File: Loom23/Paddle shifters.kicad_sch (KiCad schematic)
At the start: 0 parts

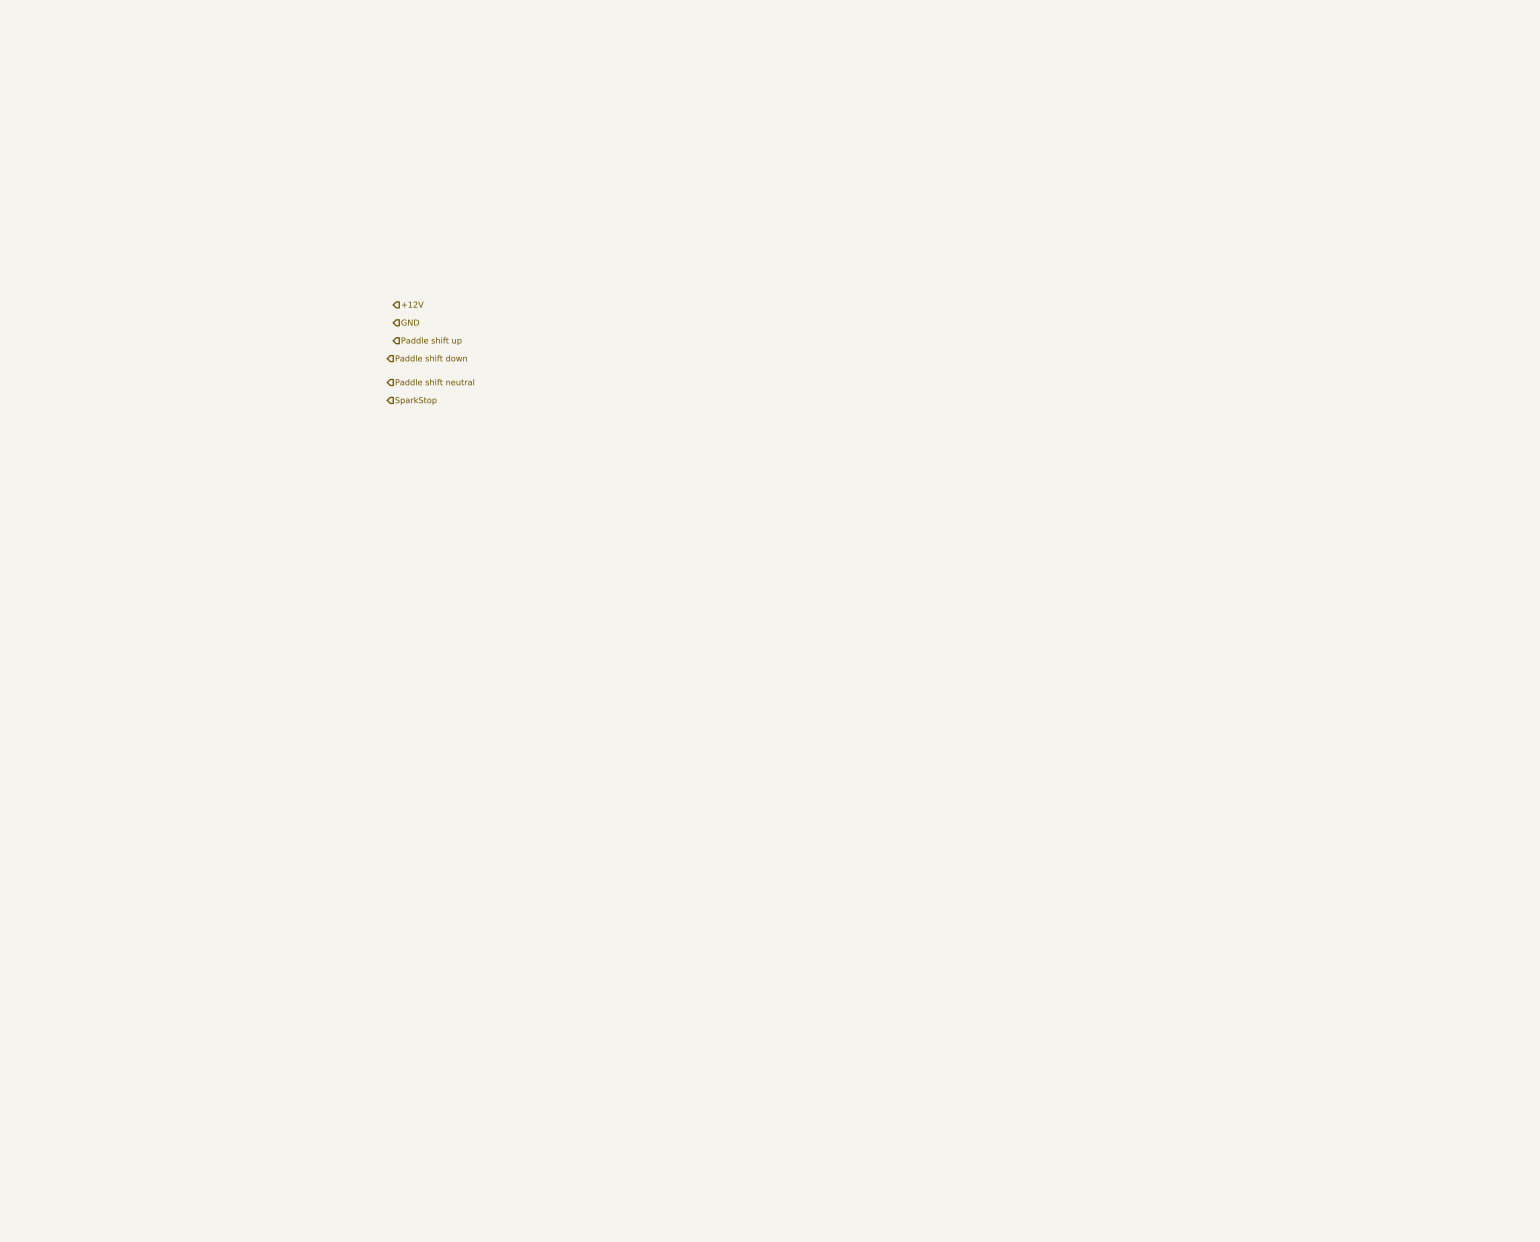
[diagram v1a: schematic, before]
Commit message: Added paddle shifter PCB and the relays.
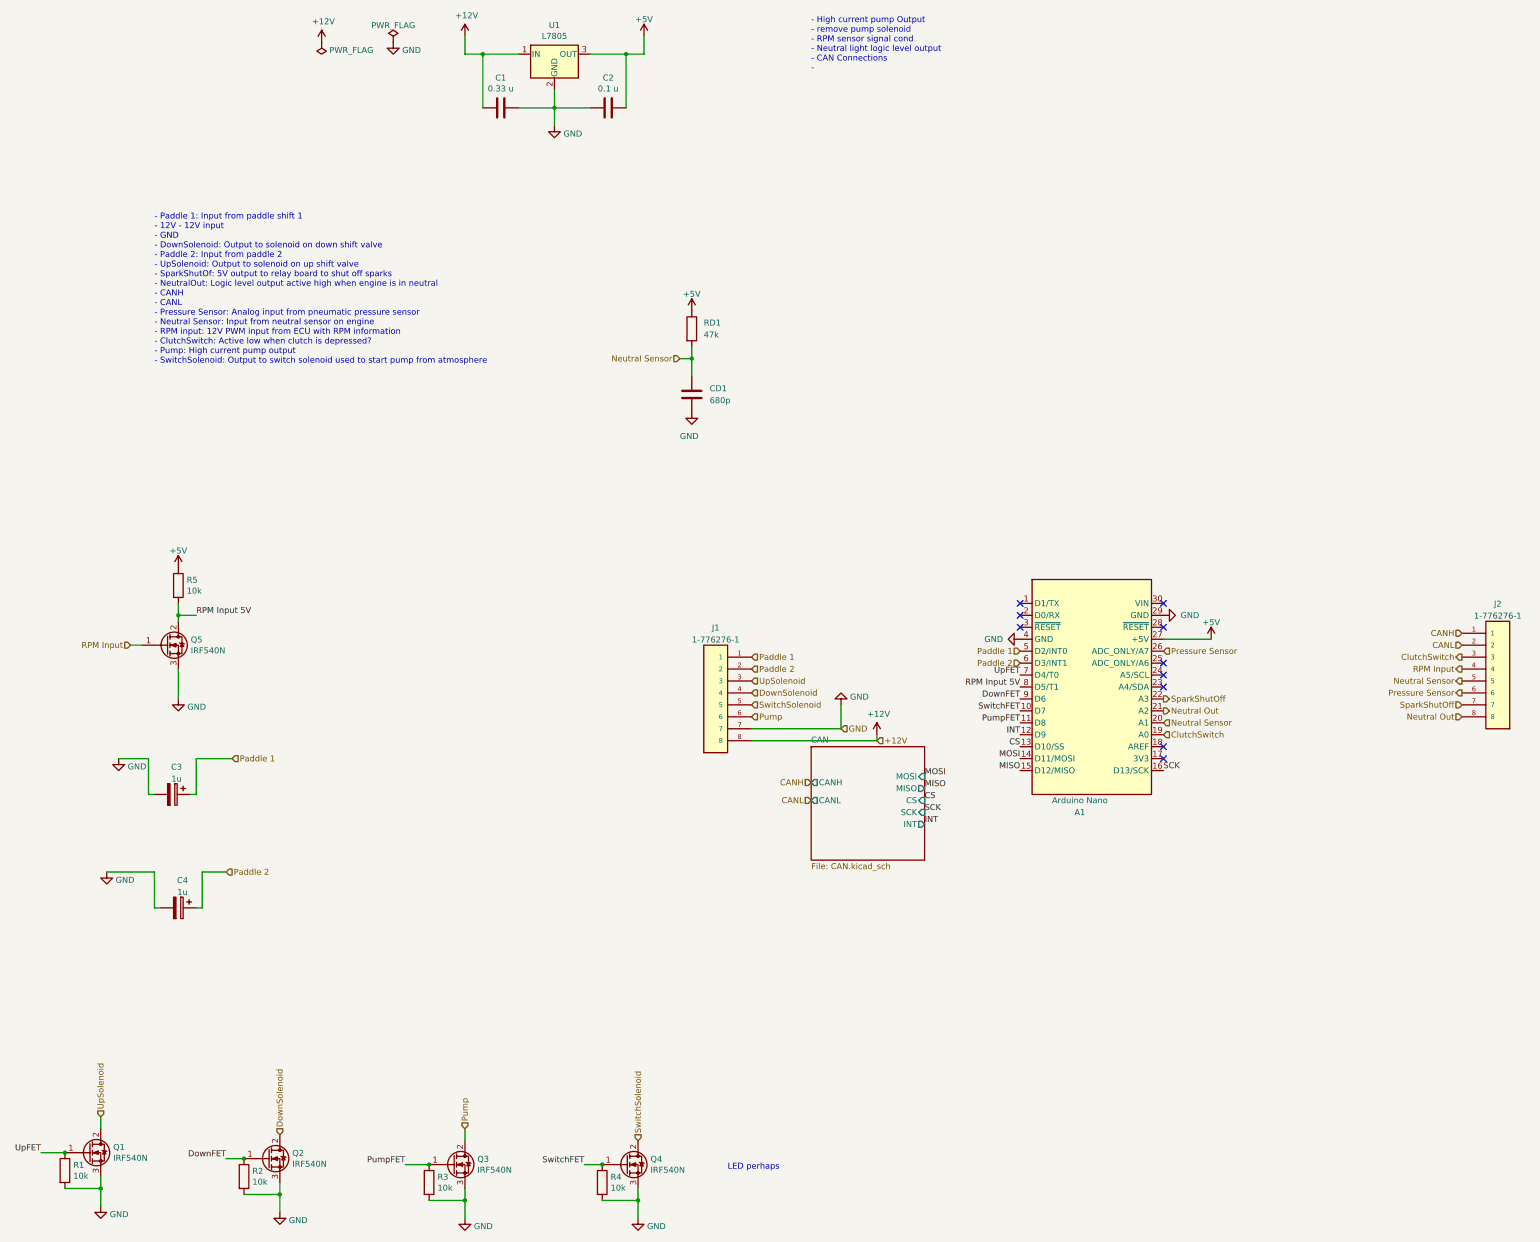
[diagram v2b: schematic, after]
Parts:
- added A1: Arduino Nano, Module:Arduino_Nano, symbol MCU_Module:Arduino_Nano_v3.x
- added C1: 0.33 u, Capacitor_THT:C_Radial_D4.0mm_H5.0mm_P1.50mm, symbol Device:C
- added C2: 0.1 u, Capacitor_THT:CP_Radial_Tantal_D4.5mm_P5.00mm, symbol Device:C
- added C3, C4: 1u, Capacitor_THT:C_Radial_D4.0mm_H5.0mm_P1.50mm, symbol Device:C_Polarized
- added CD1: 680p, Capacitor_THT:C_Disc_D5.1mm_W3.2mm_P5.00mm, symbol Device:C
- added J1: 1-776276-1, Ampseal:TE_1-776276-1, symbol Ampseal:1-776276-1
- added J2: 1-776276-1, TE_1-776276-1, symbol Ampseal:1-776276-1
- added Q1, Q2, Q3, Q4, Q5: IRF540N, Package_TO_SOT_THT:TO-220-3_Horizontal_TabDown, symbol Transistor_FET:IRF540N
- added R1, R2, R3, R4, R5: 10k, Resistor_THT:R_Axial_DIN0207_L6.3mm_D2.5mm_P7.62mm_Horizontal, symbol Device:R
- added RD1: 47k, Resistor_THT:R_Axial_DIN0207_L6.3mm_D2.5mm_P7.62mm_Horizontal, symbol Device:R
- added U1: L7805, Package_TO_SOT_THT:TO-220-3_Horizontal_TabDown, symbol Regulator_Linear:L7805
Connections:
- net +12V: now also C1.1, J1.8, U1.1 (IN)
- net GND: now also A1.29 (GND), A1.4 (GND), C1.2, C2.2, C3.2, C4.2, CD1.2, J1.7, Q1.3 (S), Q2.3 (S), Q3.3 (S), Q4.3 (S), Q5.3 (S), R1.2, R2.2, R3.2, R4.2, U1.2 (GND)
- new net +5V: A1.27 (+5V), C2.1, R5.1, RD1.1, U1.3 (OUT)
- new net CANH: J2.1
- new net CANL: J2.2
- new net CS: A1.13 (D10/SS)
- new net ClutchSwitch: A1.19 (A0), J2.3
- new net DownFET: A1.9 (D6), Q2.1 (G), R2.1
- new net DownSolenoid: J1.4, Q2.2 (D)
- new net INT: A1.12 (D9)
- new net MISO: A1.15 (D12/MISO)
- new net MOSI: A1.14 (D11/MOSI)
- new net Neutral Out: A1.21 (A2), J2.8
- new net Neutral Sensor: A1.20 (A1), CD1.1, J2.5, RD1.2
- new net Paddle 1: A1.5 (D2/INT0), C3.1, J1.1
- new net Paddle 2: A1.6 (D3/INT1), C4.1, J1.2
- new net Pressure Sensor: A1.26 (ADC_ONLY/A7), J2.6
- new net Pump: J1.6, Q3.2 (D)
- new net PumpFET: A1.11 (D8), Q3.1 (G), R3.1
- new net RPM Input: J2.4, Q5.1 (G)
- new net RPM Input 5V: A1.8 (D5/T1), Q5.2 (D), R5.2
- new net SCK: A1.16 (D13/SCK)
- new net SparkShutOff: A1.22 (A3), J2.7
- new net SwitchFET: A1.10 (D7), Q4.1 (G), R4.1
- new net SwitchSolenoid: J1.5, Q4.2 (D)
- new net UpFET: A1.7 (D4/T0), Q1.1 (G), R1.1
- new net UpSolenoid: J1.3, Q1.2 (D)
- no-connect marks 0 -> 10
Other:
- added sheet CAN (CAN.kicad_sch)
- note added: "- High current pump Output - remove pump solenoid - RPM sensor signal cond - Neutral light logic level output - CAN Connections -"
- note added: "- Paddle 1: Input from paddle shift 1 - 12V - 12V input - GND - DownSolenoid: Output to solenoid on down shift valve - Paddle 2: Input from paddle 2 - UpSolenoid: Output to solenoid on up shift valve - SparkShutOf: 5V output to relay board to shut off sparks - NeutralOut: Logic level output active high when engine is in neutral - CANH - CANL - Pressure Sensor: Analog input from pneumatic pressure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"
- note added: "LED perhaps"
